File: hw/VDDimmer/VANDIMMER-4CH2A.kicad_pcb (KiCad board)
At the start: 2 copper layers, 100 x 84 mm, 98 parts, among them J1 USB-C 16P, J10 A2 V+SEL VIN/5V, J11 BTN1, J12 BTN2, J13 EXP 3V3/GND/SDA/SCL/EN/IO0, J14 UART1 3V3/GND/TX/RX, J2 VIN 12V, J3 CH1 V+/LED-, J4 CH2 V+/LED-, J5 CH3 V+/LED-, J6 CH4 V+/LED-, J7 ADDR1 V+/D/CLK/GND, J8 ADDR2 V+/D/CLK/GND, J9 A1 V+SEL VIN/5V, Q1 20N06, Q2 20N06, Q3 20N06, Q4 20N06, Q5 SUD50P06-15, U1 ESP32-S3-WROOM-1U-N16, U2 AP63301WU-7, U3 BL1117-33CX, U4 74HCT125, U5 74HCT125

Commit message: Convert to 4 layers: sig / GND / power / sig
Adds In1.Cu and In2.Cu as plane (power-type) layers, giving the spec's
section 2 stackup: L1 signal / L2 GND / L3 power / L4 signal.

GND directly under L1 retires the Rev A "42 of 60 nets cross a pour gap"
finding structurally rather than by careful routing, and gives VIN_PROT a
plane instead of the 155 mm2 B.Cu corridor that ran through the MCU/USB
region.

Verified two ways rather than by the file's layer listing, which in KiCad 10
numbering is not in physical order (F.Cu=0, B.Cu=2, In1.Cu=4, In2.Cu=6):
  - pcbnew CuStack() reports F.Cu -> In1.Cu -> In2.Cu -> B.Cu, 4 copper layers
  - DRC before vs after, run with identical project context, is bit-identical
    across every violation class, so the layer add introduced nothing

No (setup (stackup ...)) block exists, so KiCad derives the default 4-layer
physical stackup from the layer count at the unchanged 1.6 mm thickness.

Co-Authored-By: Claude Opus 5 (1M context) <noreply@anthropic.com>
Claude-Session: https://claude.ai/code/session_01YZHVU8aymL4RkLeCfwomwj
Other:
- copper layers 2 -> 4
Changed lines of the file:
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@@
 		(35 "F.Fab" user)
 		(33 "B.Fab" user)
+		(4 "In1.Cu" power)
+		(6 "In2.Cu" power)
 	)
 	(setup

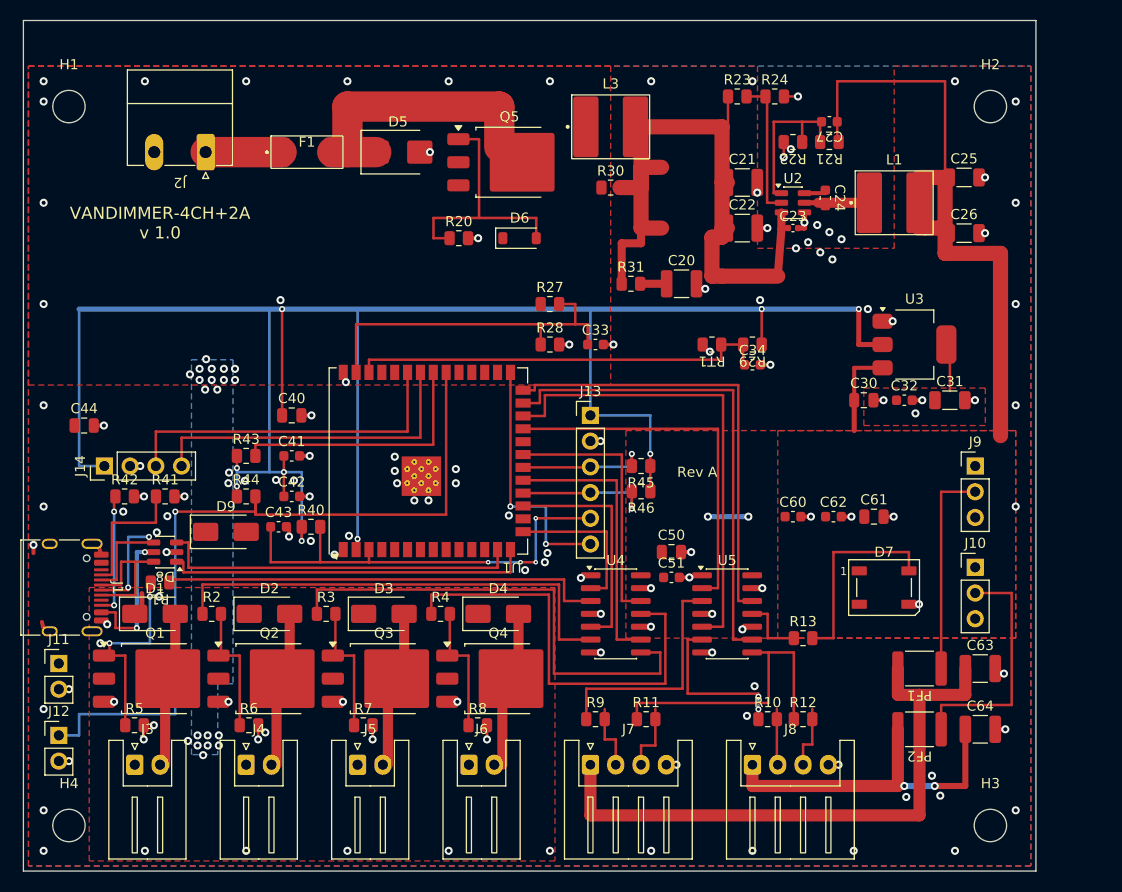
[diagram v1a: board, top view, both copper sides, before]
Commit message: Place power entry and conversion on the left edge
Rev A put power in at the north edge and outputs at the south, forcing the
~5 A VIN_PROT rail across the board through the MCU/USB region. This inverts
that: J2 sits on the left edge at (109.5, 106) rot 270 with its opening facing
the edge, and F1 -> D5 -> Q5 (Q_REV) run directly inboard of it at y 106, so
the full input current never leaves the bottom-left corner.

The buck cluster was translated RIGIDLY by (-56, +6) rather than re-placed
part by part. Rev A's Cin hot loop measured 2.51 mm2 against a 15 mm2 gate;
moving U2, C20-C24, L1, C25/C26 and the R21/R22/C27 divider as one block
preserves that geometry by construction instead of gambling on re-derivation.
measure.py confirms: loop area 2.51 mm2, 0 vias inside the loop bbox.

Connector orientation was measured, not assumed: all four connector families
on this board (JST XH 2- and 4-way, Phoenix MC, USB-C) face +y at rotation 0,
so J2 needs rot 270 to open onto the left edge.

H3 and H4 move up to y 118.5, out of the harness band. Their 5.90 mm keepouts
at y 135.5 sat exactly where J3 and J1 need to be - a collision the plan does
not anticipate. At 118.5 H4 genuinely separates J2 (courtyard bottom 114.18)
from J3 (courtyard top 126.64), which is the job spec section 5.1 gives it.

measure.py sections 2-4 still report against Rev A's stale copper (SW segments
at the old x 177-179 buck location), so those clearances are meaningless until
Phase 5 re-routes. Section 1 is the gate, and it passes.

Co-Authored-By: Claude Opus 5 (1M context) <noreply@anthropic.com>
Claude-Session: https://claude.ai/code/session_01YZHVU8aymL4RkLeCfwomwj
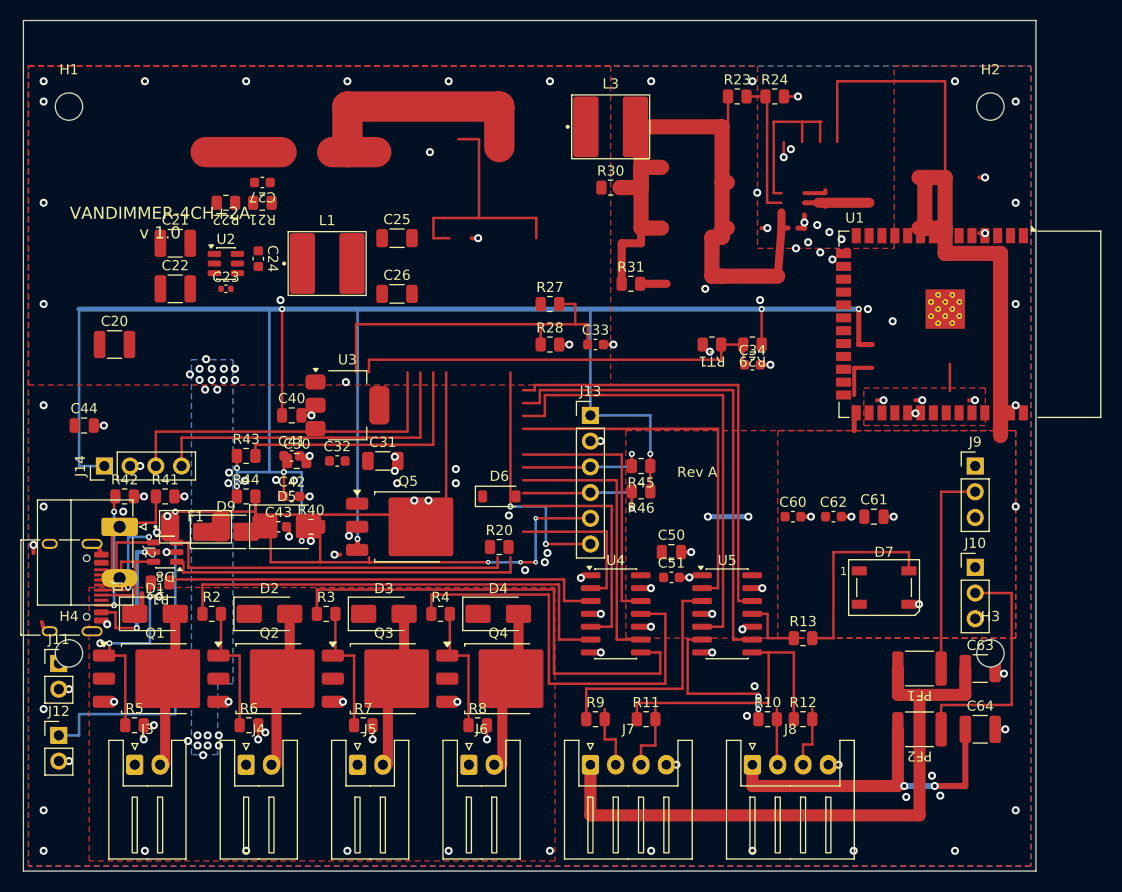
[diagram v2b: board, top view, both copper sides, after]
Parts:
- H1, H2, H3, H4: value M3 -> M2.5; footprint MountingHole:MountingHole_3.2mm_M3 -> MountingHole:MountingHole_2.7mm_M2.5
- J3: value CH1 V+/LED- -> CH1 LED-/V+
- J4: value CH2 V+/LED- -> CH2 LED-/V+
- J5: value CH3 V+/LED- -> CH3 LED-/V+
- J6: value CH4 V+/LED- -> CH4 LED-/V+
- PF1, PF2: value PTC 2A 30V -> PTC 3A 30V
- U1: value ESP32-S3-WROOM-1U-N16 -> ESP32-S3-WROOM-1-N16R8; footprint RF_Module:ESP32-S3-WROOM-1U -> RF_Module:ESP32-S3-WROOM-1
- moved C20 56.3 mm to (109.0, 88.0)
- moved C21 56.3 mm to (115.0, 78.0)
- moved C22 56.3 mm to (115.0, 82.5)
- moved C23 56.3 mm to (120.0, 82.5)
- moved C25 56.3 mm to (136.9, 77.5)
- moved C26 56.3 mm to (136.9, 83.0)
- moved C27 56.3 mm to (123.6, 72.0)
- moved C30 56.3 mm to (127.0, 99.5)
- moved C31 56.3 mm to (135.5, 99.5)
- moved C32 56.3 mm to (131.0, 99.5)
- moved L1 56.3 mm to (130.0, 80.0)
- moved R21 56.3 mm to (123.6, 74.0)
- moved R22 56.3 mm to (120.0, 74.0)
- moved U2 56.3 mm to (120.0, 80.0)
- moved U3 56.3 mm to (132.0, 94.0)
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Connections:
- J3 pad 1: VIN_PROT -> /PWM/DRAIN1
- J3 pad 2: /PWM/DRAIN1 -> VIN_PROT
- J4 pad 1: VIN_PROT -> /PWM/DRAIN2
- J4 pad 2: /PWM/DRAIN2 -> VIN_PROT
- J5 pad 1: VIN_PROT -> /PWM/DRAIN3
- J5 pad 2: /PWM/DRAIN3 -> VIN_PROT
- J6 pad 1: VIN_PROT -> /PWM/DRAIN4
- J6 pad 2: /PWM/DRAIN4 -> VIN_PROT
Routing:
- net /MCU/BOOT_IO0: track 24.0 -> 26.3 mm
- net +5V: track 78.1 -> 75.8 mm
- net unconnected-(U1-IO4-Pad4): track 0.00 -> 0.57 mm, vias 0 -> 1
- net GND: track 28.4 -> 27.9 mm, vias 141 -> 137
- net unconnected-(U1-IO14-Pad22): vias 0 -> 1
- net GATE_IN1: vias 0 -> 1
- net /Power/VIN_FUSED: vias 0 -> 1
